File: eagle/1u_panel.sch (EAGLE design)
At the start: 33 parts, among them U1 SPV1040, U5 ONP-CHANNEL, U6 ON-N-CHANNEL-FET, U7 DIODE-INC-NPN, U8 ON-TVS-ARRAY, U9 ON-TVS-ARRAY

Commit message: Finished preliminary board layout
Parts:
- U5: value ONP-CHANNEL -> P-CHANNELFET; device on-p-channel-fet:ONP-CHANNEL -> vishay-p-channel-fet:P-CHANNELFET
- renumbered U9 to SHORT
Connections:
- net ADR1: now also CM1.19
- net GND: now also CM1.10, CM1.21, CM1.22, CM1.23, CM1.24, CM1.9
- net SCL: now also CM1.15
- net SDA: now also CM1.3
- net SHORT: now also CM1.5
- net VCC: now also CM1.7
- net VSOLAR: now also CM1.11, CM1.12, CM1.13, CM1.14
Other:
- moved on the sheet: CM1

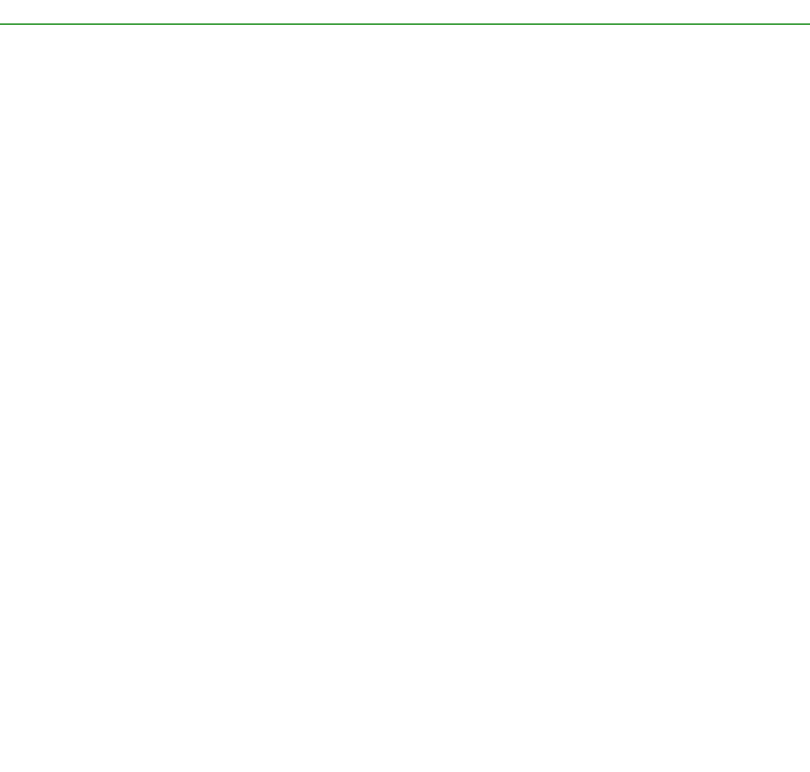
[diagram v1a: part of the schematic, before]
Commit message: Added STM32 MCU
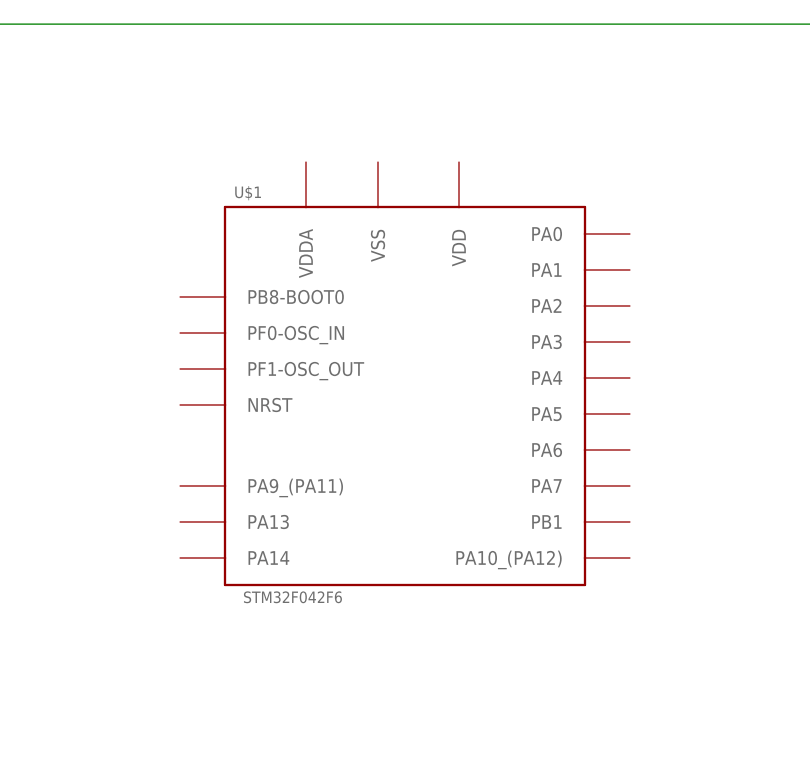
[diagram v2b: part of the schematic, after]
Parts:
- added U$1: STM32F042F6, STM32F042F6:STM32F042F6
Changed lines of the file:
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@@
 <part name="L2" library="inductor-for-spv" deviceset="L" device="PIS2816"/>
 <part name="CM1" library="oresat-eagle" deviceset="ORESAT-BACKPLANE-40PIN" device=""/>
+<part name="U$1" library="STM32F042F6" deviceset="STM32F042F6" device=""/>
 </parts>
 <sheets>
@@
 <instance part="L2" gate="G$1" x="114.3" y="198.12" rot="R270"/>
 <instance part="CM1" gate="G$1" x="414.02" y="189.23" rot="MR0"/>
+<instance part="U$1" gate="G$1" x="175.26" y="116.84"/>
 </instances>
 <busses>

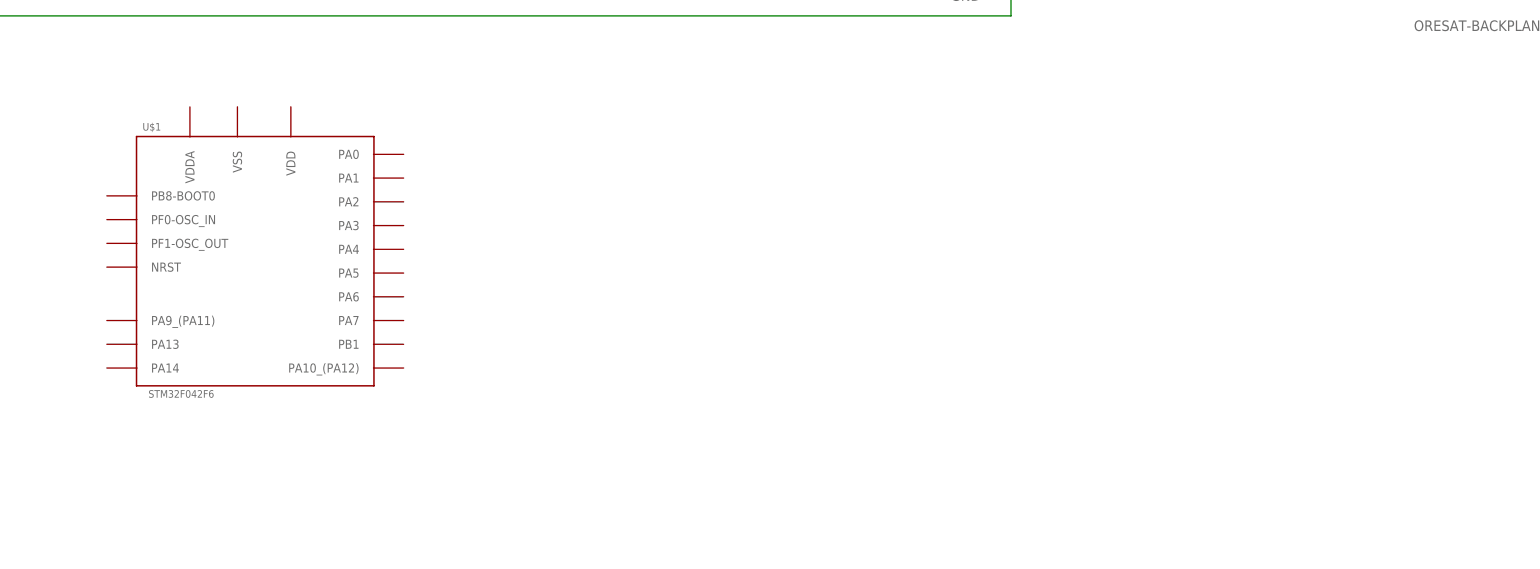
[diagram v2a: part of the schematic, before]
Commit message: Added symbols and footprints to drawing.
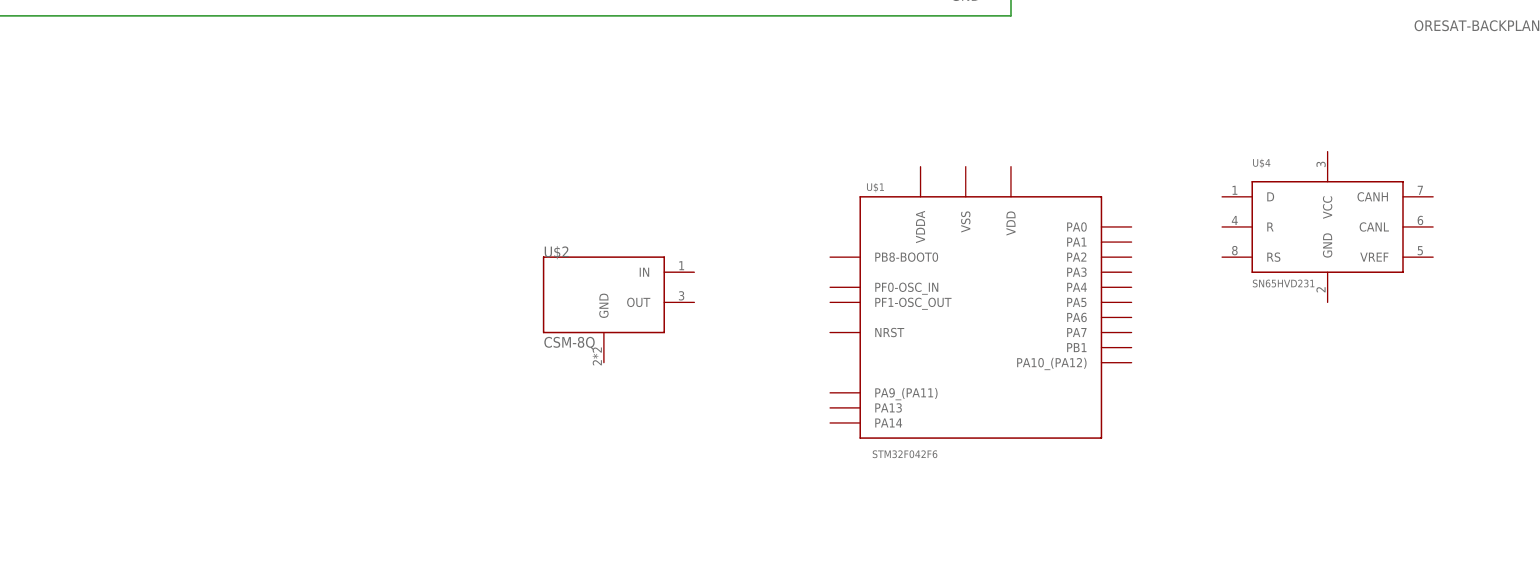
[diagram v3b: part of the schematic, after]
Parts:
- added U$2: CSM-8Q, CSM-8Q:CSM-8Q
- added U$4: SN65HVD231, SN65HVD231:SN65HVD231
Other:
- moved on the sheet: U$1
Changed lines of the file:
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@@
 <part name="L2" library="inductor-for-spv" deviceset="L" device="PIS2816"/>
 <part name="CM1" library="oresat-eagle" deviceset="ORESAT-BACKPLANE-40PIN" device=""/>
+<part name="U$2" library="CSM-8Q" deviceset="CSM-8Q" device=""/>
 <part name="U$1" library="STM32F042F6" deviceset="STM32F042F6" device=""/>
+<part name="U$4" library="SN65HVD231" deviceset="SN65HVD231" device=""/>
 </parts>
 <sheets>
@@
 <instance part="L2" gate="G$1" x="114.3" y="198.12" rot="R270"/>
 <instance part="CM1" gate="G$1" x="414.02" y="189.23" rot="MR0"/>
-<instance part="U$1" gate="G$1" x="175.26" y="116.84"/>
+<instance part="U$2" gate="G$1" x="254" y="91.44"/>
+<instance part="U$1" gate="G$1" x="317.5" y="86.36"/>
+<instance part="U$4" gate="G$1" x="375.92" y="99.06"/>
 </instances>
 <busses>

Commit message: Nets, Caps, GND oh my.
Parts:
- added C11, C16, C17, C3, C9: (no value), rcl:C-EUC0603
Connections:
- removed net SCL: CM1.15, U$3.SCL, U8D.1
- removed net SDA: CM1.3, U$3.SDA, U8C.1
- new net 3.3V: C17.2, C3.2, C9.2, CM1.37, CM1.38, U$1.PB8-BOOT0, U$1.VDD, U$1.VDDA, U$4.VCC
- new net CAND: U$1.PA10_(PA12), U$4.D
- new net CANH: CM1.39, U$4.CANH
- new net CANL: CM1.40, U$4.CANL
- new net CANR: U$1.PA9_(PA11), U$4.R
- new net CRYSTALIN: C16.1, U$1.PF0-OSC_IN, U$2.IN
- new net CRYSTALOUT: C11.1, U$1.PF1-OSC_OUT, U$2.OUT
- new net N$1: CM1.36, U$1.NRST
- new net N$2: U$3.ADR1
- net ADR1: no longer SHORTA.1, U$3.ADR1
- net GND: now also C11.2, C16.2, C17.1, C3.1, C9.1, U$1.VSS, U$2.GND, U$4.GND, U$4.RS
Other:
- note added: "N/C"
- note added: "TODO New Lib for upside down transistor New Package for P-Channel Fet Finish connecting outputs Draw Polygons Design ignoring layers 2 and 15 Change to QFN MCU ADD super low power buck regulator that takes 5.5V max in and makes 3.3V and can do like ~ 100 mA and has a voltage divider to provide a low-voltage disable"
- note removed: "TODO New Lib for upside down transistor New Package for P-Channel Fet Finish connecting outputs Draw Polygons Design ignoring layers 2 and 15"
- moved on the sheet: U$1, U$2, U$4

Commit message: Added new MCU to board attached I2C, crystal and can nets
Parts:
- added C18, C19: (no value), rcl:C-EUC0603
- U$1: value STM32F042F6 -> STM32F042; device STM32F042F6:STM32F042F6 -> STM32F042F6:STM32F042
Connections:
- removed net CAND: U$1.PA10_(PA12), U$4.D
- removed net CANR: U$1.PA9_(PA11), U$4.R
- new net N$3: U$1.PB6, U$3.SCL
- new net N$4: U$1.PB7, U$3.SDA
- new net N$5: C19.1, U$1.PA10_(PA12), U$4.D
- new net N$6: C18.1, U$1.PA9_(PA11), U$4.R
- net GND: now also C18.2, C19.2
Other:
- note added: "SCL"
- note added: "SDA"
- moved on the sheet: C17, C3, C9, SHORTA, SHORTB, U$4, U8A, U8B, U8C, U8D

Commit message: Pushing changes from Space Electronics workshop - no more TVS diodes, need onboard regulator, etc.
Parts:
- added R11: 0, rcl_custom:R-US_0603-B-NOSILK
- added R12: (no value), rcl_custom:R-US_0603-B-NOSILK
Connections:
- removed net 3.3V: C17.2, C3.2, C9.2, CM1.37, CM1.38, U$1.PB8-BOOT0, U$1.VDD, U$1.VDDA, U$4.VCC
- removed net ADR1: CM1.19
- removed net VCC: CM1.7, U$3.VCC, U8B.1
- new net N$10: C3.2, C9.2, U$1.PB8-BOOT0, U$1.VDD, U$1.VDDA
- new net N$7: U$3.VCC
- new net N$8: R12.1, U$3.ADR1
- new net N$9: C17.2, U$4.VCC
- net GND: now also R11.2, R12.2; no longer SHORTC.1, U$4.RS
- net N$2: now also R11.1, U$4.RS; no longer U$3.ADR1
- net SHORT: no longer SHORTB.1
- net VSOLAR: no longer U8A.1
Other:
- note added: "Low power mode? Babble mode?"
- note added: "POWER ME"

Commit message: Added LM3761, removed TPS arrays, adjusted schematic symbols to clean up drawings
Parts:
- removed SHORT, U8: ON-TVS-ARRAY, on-tvs-diode-array:ON-TVS-ARRAY
- added C20, C21: 4.7u, rcl:C-EUC0603
- added L1: 10u, rcl:L-USL2012C
- added R13, R14: 10k, rcl:R-US_R0603
- added U$5: LM3761, LM3761:LM3761
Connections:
- removed net CANH: CM1.39, U$4.CANH
- removed net CANL: CM1.40, U$4.CANL
- removed net N$3: U$1.PB6, U$3.SCL
- removed net N$4: U$1.PB7, U$3.SDA
- new net 3.3V: C17.2, C21.1, C3.2, C9.2, L1.1, U$1.PB8-BOOT0, U$1.VDD, U$1.VDDA, U$3.VCC, U$4.VCC, U$5.FB
- new net N$11: L1.2, U$5.SW
- new net N$12: CM1.8, U$4.CANL
- new net N$15: R13.1, R14.2, U$5.EN
- net GND: now also C20.2, C21.2, CM1.11, CM1.12, R14.1, U$5.GND; no longer CM1.21, CM1.22, CM1.23, CM1.24, SHORTG$5.GND, U8G$5.GND
- net N$1: now also U$1.PB7, U$3.SCL; no longer CM1.36, U$1.NRST
- net N$10: now also CM1.6, U$4.CANH; no longer C3.2, C9.2, U$1.PB8-BOOT0, U$1.VDD, U$1.VDDA
- net N$7: now also U$1.PB6, U$3.SDA; no longer U$3.VCC
- net N$9: now also U$1.NRST; no longer C17.2, U$4.VCC
- net SHORT: now also CM1.1; no longer CM1.5
- net SOLAR-IN-SWITCHED1: now also C20.1, R13.2, U$5.VIN
- net VSOLAR: now also CM1.2, CM1.3, CM1.4, CM1.5; no longer CM1.11, CM1.12, CM1.13, CM1.14
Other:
- note removed: "POWER ME"
- moved on the sheet: C11, C16, C17, C18, C19, C3, C9, CM1, R1, R10, R11, R12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

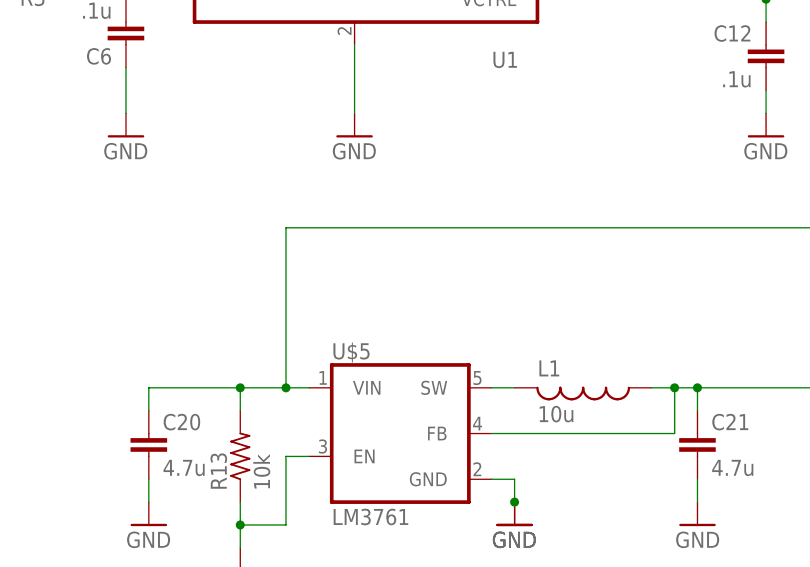
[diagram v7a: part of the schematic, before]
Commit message: Added net annotations
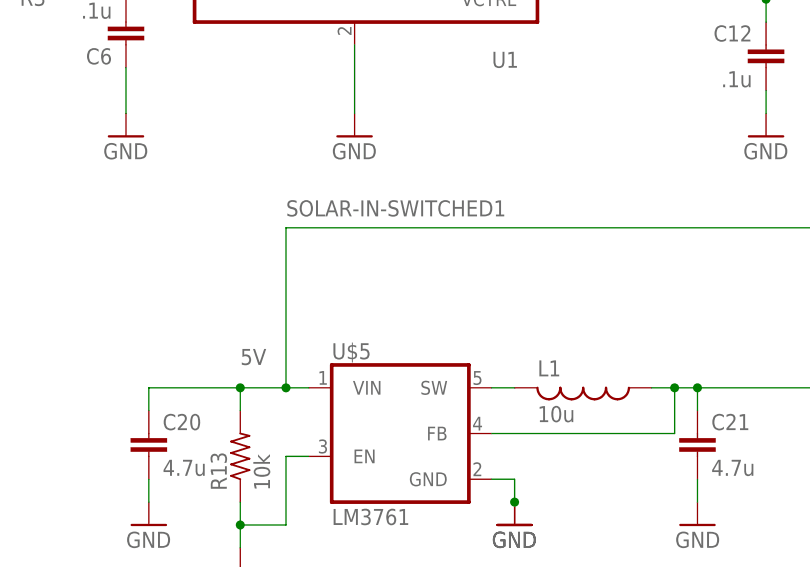
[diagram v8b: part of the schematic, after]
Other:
- note added: "5V"
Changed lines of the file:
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@@
 Babble mode?
 </text>
+<text x="137.16" y="142.24" size="1.778" layer="95">5V</text>
 </plain>
 <instances>
@@
 <wire x1="241.3" y1="157.48" x2="241.3" y2="208.28" width="0.1524" layer="91"/>
 <junction x="241.3" y="208.28"/>
-</segment>
-</net>
+<label x="142.24" y="158.75" size="1.778" layer="95"/>
+</segment>
+</net>
